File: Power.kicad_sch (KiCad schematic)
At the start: 25 parts, among them IC1 SC4216HSETRT, J4 Conn_01x03, J5 Conn_01x02, U8 TPS62933P

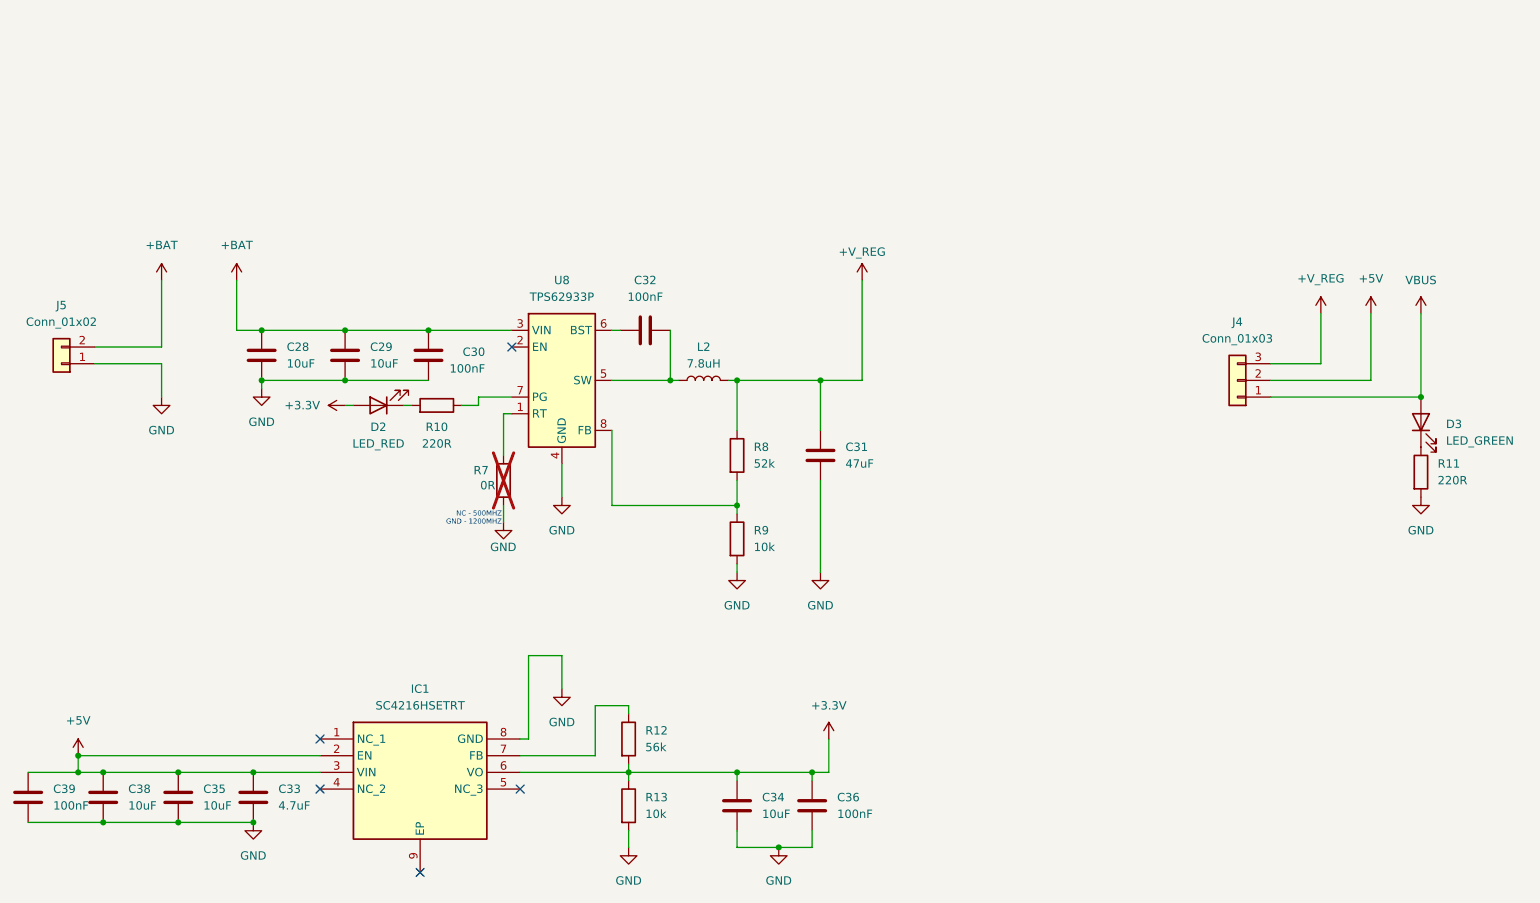
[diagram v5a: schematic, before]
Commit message: Fix
- Add decoupling cap
- Component layout
- Redraw zones
- New buck converter
- Layout tweaks
- Change connector
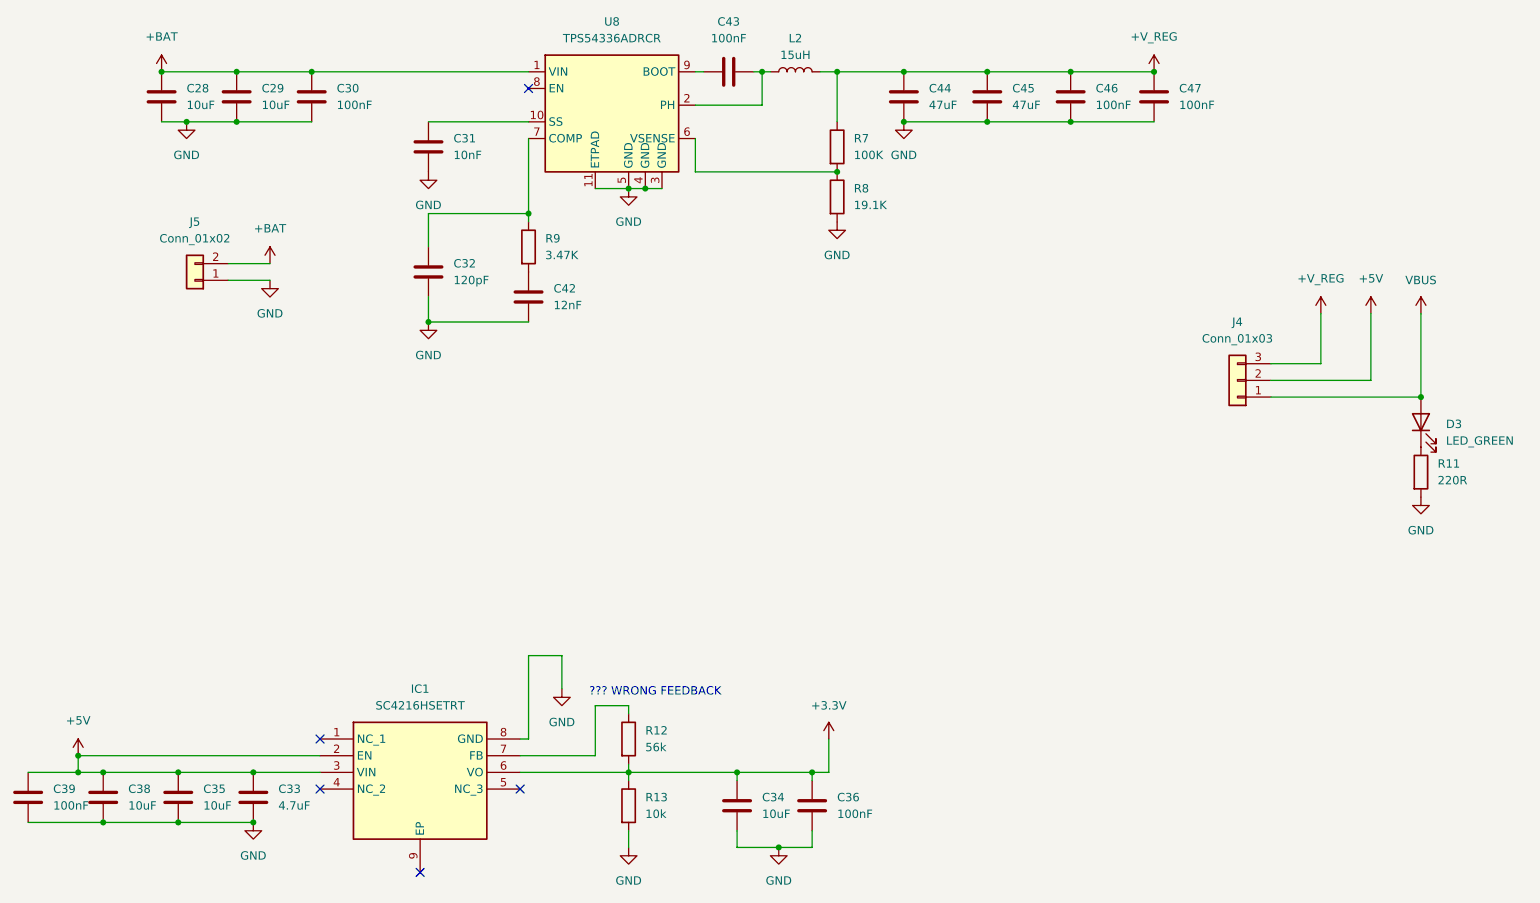
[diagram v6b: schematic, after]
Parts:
- removed D2: LED_RED, LED_SMD:LED_0603_1608Metric, symbol Device:LED
- removed R10: 220R, Resistor_SMD:R_0402_1005Metric, symbol Device:R
- removed U8: TPS62933P, Package_TO_SOT_SMD:SOT-583-8, symbol Regulator_Switching:TPS62933P
- added C42: 12nF, Capacitor_SMD:C_0603_1608Metric, symbol Device:C
- added C43, C46, C47: 100nF, Capacitor_SMD:C_0603_1608Metric, symbol Device:C
- added C44, C45: 47uF, Capacitor_SMD:C_1210_3225Metric, symbol Device:C
- added U8: TPS54336ADRCR, Package_SON:VSON-10-1EP_3x3mm_P0.5mm_EP1.65x2.4mm_ThermalVias, symbol Regulator_Switching:TPS54336ADRCR
- C28: footprint Capacitor_SMD:C_1206_3216Metric -> Capacitor_SMD:C_1210_3225Metric; Source https://www.lcsc.com/product-detail/C89632.html -> (none)
- C29: footprint Capacitor_SMD:C_1206_3216Metric -> Capacitor_SMD:C_1210_3225Metric
- C30: Source https://www.lcsc.com/product-detail/C1591.html -> (none)
- C31: value 47uF -> 10nF; footprint Capacitor_SMD:C_1210_3225Metric -> Capacitor_SMD:C_0603_1608Metric
- C32: value 100nF -> 120pF
- J4: footprint Connector_PinSocket_2.54mm:PinSocket_1x03_P2.54mm_Vertical -> Connector_PinHeader_2.54mm:PinHeader_1x03_P2.54mm_Vertical
- L2: value 7.8uH -> 15uH; footprint Inductor_SMD:L_APV_APH1050 -> Inductor_SMD:L_Bourns-SRN8040_8x8.15mm
- R7: value 0R -> 100K; now fitted
- R8: value 52k -> 19.1K; footprint Resistor_SMD:R_0805_2012Metric -> Resistor_SMD:R_0603_1608Metric
- R9: value 10k -> 3.47K
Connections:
- net +BAT: now also U8.1 (VIN)
- net +V_REG: now also R7.1, C44.1, C45.1, C46.1, C47.1; no longer C31.1, R8.1
- net GND: now also C32.2, R8.2, C42.2, C44.2, C45.2, C46.2, C47.2, U8.11 (ETPAD), U8.3 (GND), U8.4 (GND), U8.5 (GND); no longer R7.2, R9.2
- net at L2.1: now also C43.2, U8.2 (PH); no longer C32.2
- net at C32.1: now also R9.1, U8.7 (COMP)
- new net: C43.1, U8.9 (BOOT)
- new net: C31.1, U8.10 (SS)
- new net: R7.2, R8.1, U8.6 (VSENSE)
- new net: C42.1, R9.2
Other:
- note added: "??? WRONG FEEDBACK"
- note removed: "NC - 500MHZ GND - 1200MHZ"
- moved on the sheet: J5
